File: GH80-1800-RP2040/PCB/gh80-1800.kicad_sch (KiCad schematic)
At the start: 280 parts, among them J1 USB_mini_micro_B, J2 ISP, J3 USB Header, J4 USB_mini_micro_B, J5 USB_mini_micro_B, K1 KEYSW, K10 KEYSW, K100 KEYSW, K101 KEYSW, K102 KEYSW, K103 KEYSW, K104 KEYSW, K105 KEYSW, K107 KEYSW, K108 KEYSW, K109 KEYSW, K11 KEYSW, K110 KEYSW, K12 KEYSW, K13 KEYSW, K14 KEYSW, K15 KEYSW, K16 KEYSW, K17 KEYSW, K18 KEYSW, K18-1 KEYSW, K19 KEYSW, K2 KEYSW, K20 KEYSW, K21 KEYSW, K22 KEYSW, K23 KEYSW, K24 KEYSW, K25 KEYSW, K26 KEYSW, K27 KEYSW, K28 KEYSW, K29 KEYSW, K3 KEYSW, K30 KEYSW, K31 KEYSW, K32 KEYSW, K33 KEYSW, K34 KEYSW, K35 KEYSW, K36 KEYSW, K37 KEYSW, K38 KEYSW, K39 KEYSW, K4 KEYSW, K40 KEYSW, K41 KEYSW, K42 KEYSW, K43 KEYSW, K44 KEYSW, K45 KEYSW, K46 KEYSW, K47 KEYSW, K48 KEYSW, K49 KEYSW, K5 KEYSW, K50 KEYSW, K51 KEYSW, K52 KEYSW, K53 KEYSW, K54 KEYSW, K55 KEYSW, K55-1 KEYSW, K56 KEYSW, K57 KEYSW, K58 KEYSW, K59 KEYSW, K6 KEYSW, K60 KEYSW, K61 KEYSW, K62 KEYSW, K63 KEYSW, K64 KEYSW, K65 KEYSW, K66 KEYSW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

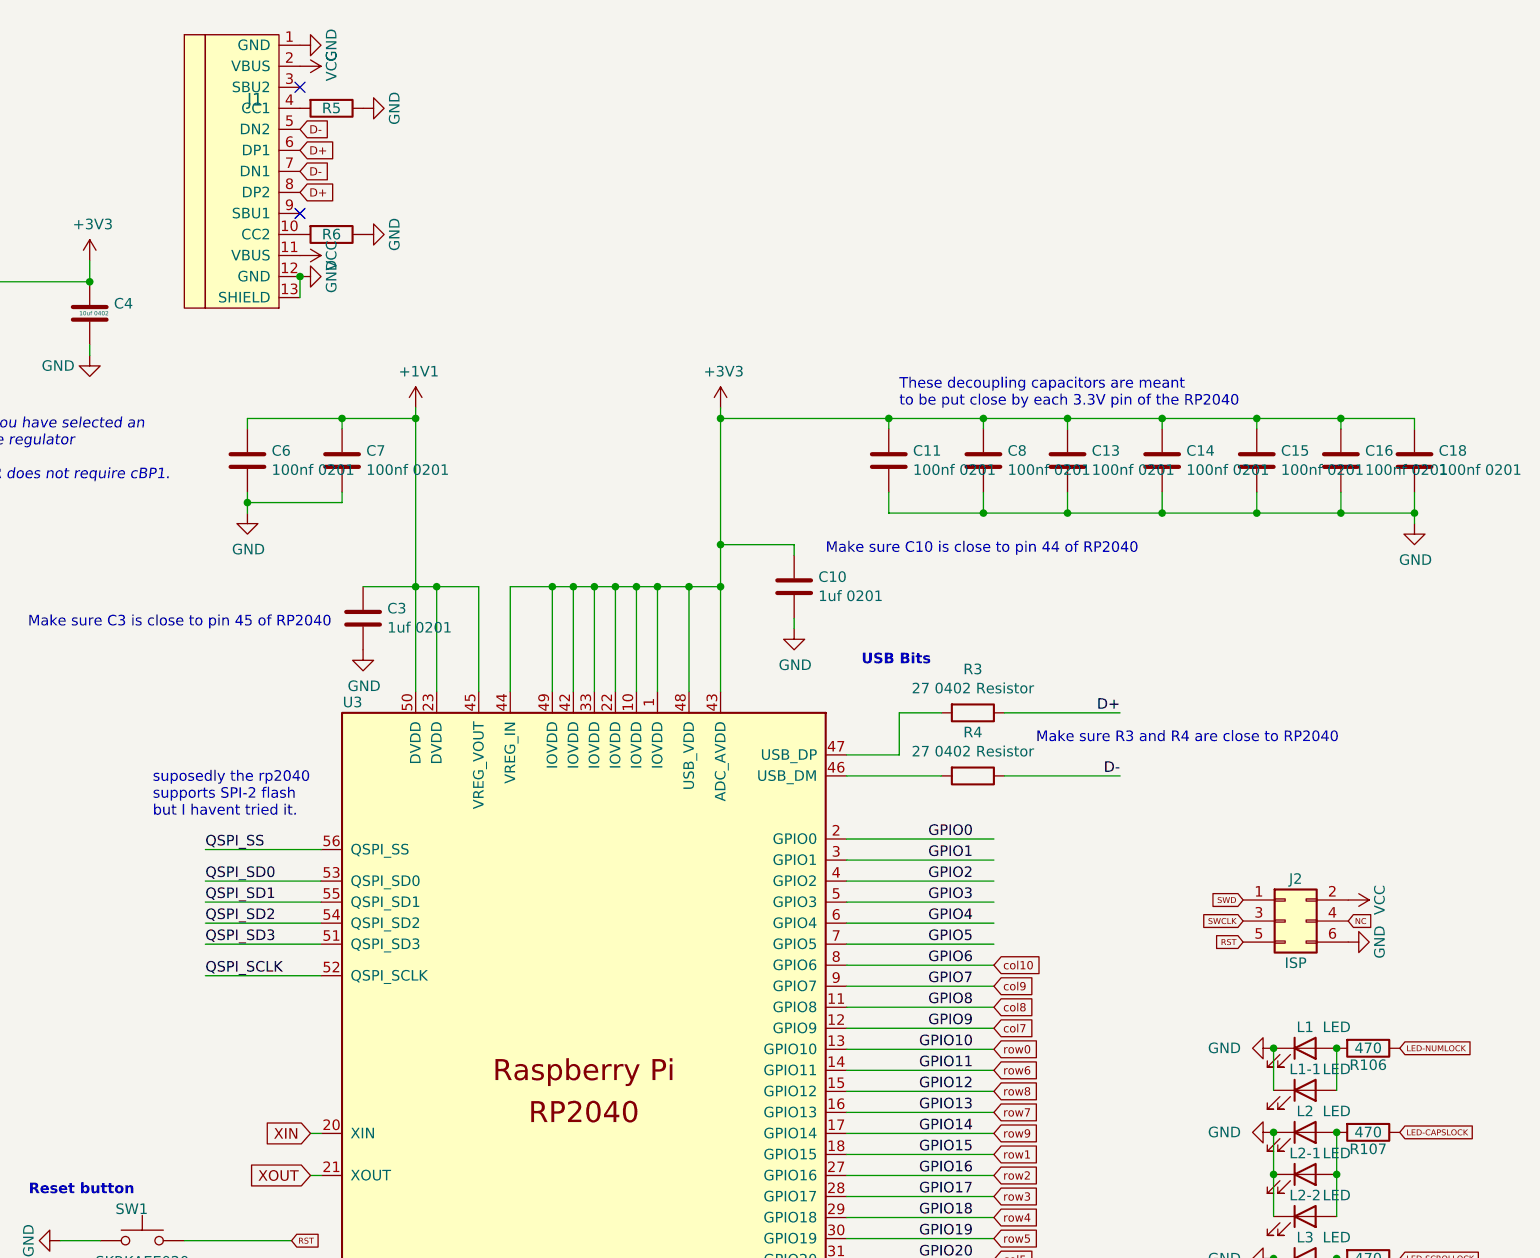
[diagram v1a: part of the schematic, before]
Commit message: remove unused bits from circuit
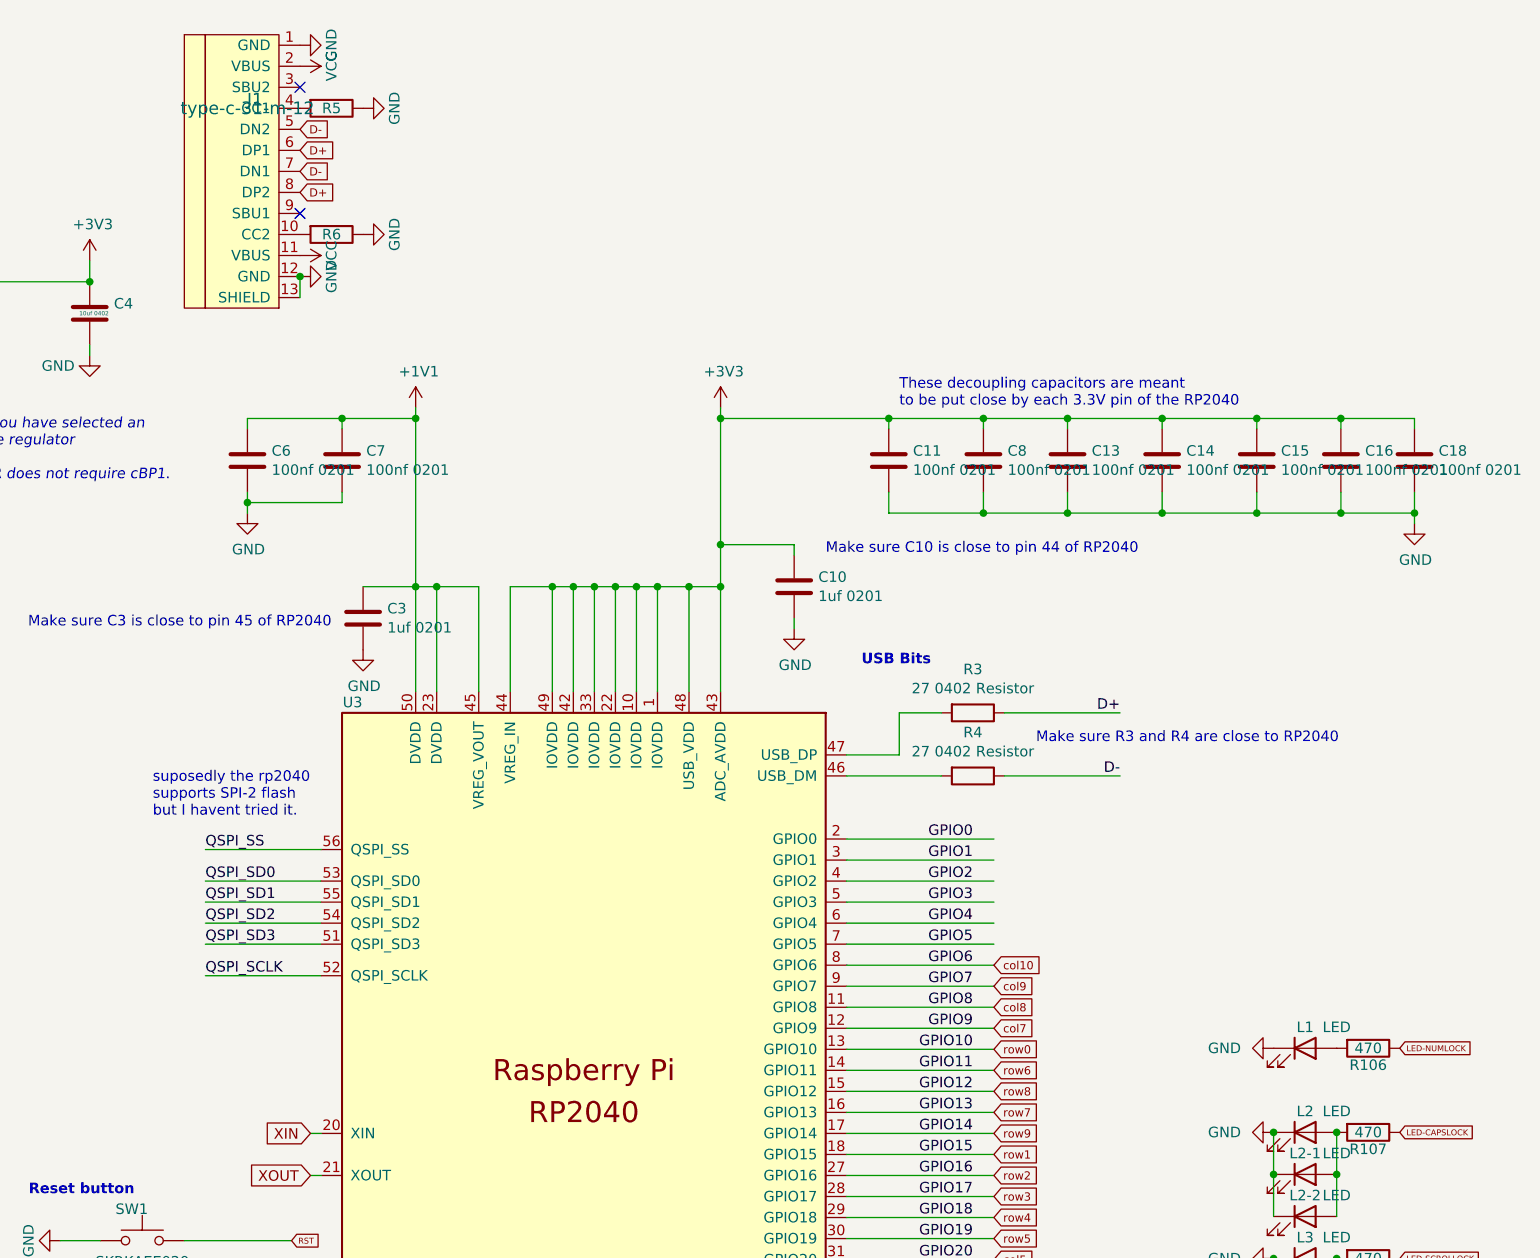
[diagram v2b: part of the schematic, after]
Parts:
- removed J2: ISP, Keeb_components:isp_standard, symbol Connector_Generic:Conn_02x03_Odd_Even
- removed L1-1: LED, Keeb_switches:CHERRY_MX_LED, symbol Device:LED
- J1: value USB_mini_micro_B -> type-c-31-m-12
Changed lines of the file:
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@@
   (junction (at 191.135 454.025) (diameter 0) (color 0 0 0 0)
   )
-  (junction (at 281.432 137.033) (diameter 0) (color 0 0 0 0)
-  )
   (junction (at 310.515 461.645) (diameter 0) (color 0 0 0 0)
   )
@@
   (junction (at 114.935 390.525) (diameter 0) (color 0 0 0 0)
   )
-  (junction (at 289.052 137.033) (diameter 0) (color 0 0 0 0)
-  )
   (junction (at 310.515 377.825) (diameter 0) (color 0 0 0 0)
   )
@@
     (stroke (width 0) (type default) (color 0 0 0 0))
   )
-  (wire (pts (xy 281.432 142.113) (xy 281.432 137.033))
-    (stroke (width 0) (type default) (color 0 0 0 0))
-  )
   (wire (pts (xy 353.695 471.805) (xy 353.695 476.885))
     (stroke (width 0) (type default) (color 0 0 0 0))
@@
     (stroke (width 0) (type default) (color 0 0 0 0))
   )
-  (wire (pts (xy 289.052 142.113) (xy 289.052 137.033))
-    (stroke (width 0) (type default) (color 0 0 0 0))
-  )
   (wire (pts (xy 254.635 390.525) (xy 226.695 390.525))
     (stroke (width 0) (type default) (color 0 0 0 0))
@@
     )
   )
-  (global_label "RST" (shape input) (at 277.749 124.206 180)
-    (effects (font (size 0.7112 0.7112)) (justify right))
-    (property "Intersheet References" "${INTERSHEET_REFS}" (id 0) (at 44.069 73.406 0)
-      (effects (font (size 1.27 1.27)) hide)
-    )
-  )
   (global_label "col2" (shape input) (at 163.195 332.105 0)
     (effects (font (size 1.4986 1.4986)) (justify left))
@@
     )
   )
-  (global_label "NC" (shape input) (at 290.449 121.666 0)
-    (effects (font (size 0.7112 0.7112)) (justify left))
-    (property "Intersheet References" "${INTERSHEET_REFS}" (id 0) (at 44.069 73.406 0)
-      (effects (font (size 0.7112 0.7112)) hide)
-    )
-  )
   (global_label "row4" (shape input) (at 247.65 157.48 0)
     (effects (font (size 0.9906 0.9906)) (justify left))
@@
     )
   )
-  (global_label "SWD" (shape input) (at 277.749 119.126 180)
-    (effects (font (size 0.7112 0.7112)) (justify right))
-    (property "Intersheet References" "${INTERSHEET_REFS}" (id 0) (at 44.069 73.406 0)
-      (effects (font (size 0.7112 0.7112)) hide)
-    )
-  )
   (global_label "VSYS" (shape input) (at 66.04 44.45 0) (fields_autoplaced)
     (effects (font (size 0.508 0.508)) (justify left))
@@
     )
   )
-  (global_label "SWCLK" (shape input) (at 277.749 121.666 180)
-    (effects (font (size 0.7112 0.7112)) (justify right))
-    (property "Intersheet References" "${INTERSHEET_REFS}" (id 0) (at 44.069 73.406 0)
-      (effects (font (size 0.7112 0.7112)) hide)
-    )
-  )
   (global_label "XIN" (shape input) (at 165.1 147.32 180) (fields_autoplaced)
     (effects (font (size 1.27 1.27)) (justify right))
@@
     (pin "1")
   )
-  (symbol (lib_id "Power:GND") (at 290.449 124.206 90) (unit 1)
-    (in_bom yes) (on_board yes)
-    (property "Reference" "#PWR010" (id 0) (at 296.799 124.206 0)
-      (effects (font (size 1.27 1.27)) hide)
-    )
-    (property "Value" "GND" (id 1) (at 294.259 124.206 0))
-    (property "Footprint" "" (id 2) (at 290.449 124.206 0)
-      (effects (font (size 1.27 1.27)) hide)
-    )
-    (property "Datasheet" "" (id 3) (at 290.449 124.206 0)
-      (effects (font (size 1.27 1.27)) hide)
-    )
-    (pin "1")
-  )
-  (symbol (lib_id "Power:VCC") (at 290.449 119.126 270) (unit 1)
-    (in_bom yes) (on_board yes)
-    (property "Reference" "#PWR011" (id 0) (at 286.639 119.126 0)
-      (effects (font (size 1.27 1.27)) hide)
-    )
-    (property "Value" "VCC" (id 1) (at 294.259 119.126 0))
-    (property "Footprint" "" (id 2) (at 290.449 119.126 0)
-      (effects (font (size 1.27 1.27)) hide)
-    )
-    (property "Datasheet" "" (id 3) (at 290.449 119.126 0)
-      (effects (font (size 1.27 1.27)) hide)
-    )
-    (pin "1")
-  )
-  (symbol (lib_id "Connector_Generic:Conn_02x03_Odd_Even") (at 282.829 121.666 0) (unit 1)
-    (in_bom yes) (on_board yes)
-    (property "Reference" "J2" (id 0) (at 284.099 116.586 0))
-    (property "Value" "ISP" (id 1) (at 284.099 126.746 0))
-    (property "Footprint" "Keeb_components:isp_standard" (id 2) (at 282.829 121.666 0)
-      (effects (font (size 1.27 1.27)) hide)
-    )
-    (property "Datasheet" "" (id 3) (at 282.829 121.666 0)
-      (effects (font (size 1.27 1.27)) hide)
-    )
-    (pin "1")
-    (pin "2")
-    (pin "3")
-    (pin "4")
-    (pin "5")
-    (pin "6")
-  )
   (symbol (lib_id "Device:LED") (at 285.242 137.033 0) (unit 1)
     (in_bom yes) (on_board yes)
@@
       (effects (font (size 1.524 1.524)))
     )
-    (property "Value" "USB_mini_micro_B" (id 1) (at 157.48 23.495 0)
-      (effects (font (size 1.524 1.524)) hide)
+    (property "Value" "type-c-31-m-12" (id 1) (at 157.48 23.495 0)
+      (effects (font (size 1.524 1.524)))
     )
     (property "Footprint" "Type-C:HRO-TYPE-C-31-M-12" (id 2) (at 161.29 29.845 0)
@@
     (pin "2")
   )
-  (symbol (lib_id "Device:LED") (at 285.242 142.113 0) (unit 1)
-    (in_bom yes) (on_board yes)
-    (property "Reference" "L1-1" (id 0) (at 285.242 139.573 0))
-    (property "Value" "LED" (id 1) (at 289.052 139.573 0))
-    (property "Footprint" "Keeb_switches:CHERRY_MX_LED" (id 2) (at 285.242 142.113 0)
-      (effects (font (size 1.27 1.27)) hide)
-    )
-    (property "Datasheet" "" (id 3) (at 285.242 142.113 0)
-      (effects (font (size 1.27 1.27)) hide)
-    )
-    (pin "1")
-    (pin "2")
-  )
   (symbol (lib_id "keyboard_parts:KEYSW") (at 374.015 426.085 0) (unit 1)
     (in_bom yes) (on_board yes)
@@
       (reference "#PWR09") (unit 1) (value "+3V3") (footprint "")
     )
-    (path "/00000000-0000-0000-0000-000059ee9bff"
-      (reference "#PWR010") (unit 1) (value "GND") (footprint "")
-    )
-    (path "/00000000-0000-0000-0000-000059ee9e32"
-      (reference "#PWR011") (unit 1) (value "VCC") (footprint "")
-    )
     (path "/00000000-0000-0000-0000-00005edc8ac7"
       (reference "#PWR015") (unit 1) (value "GND") (footprint "")
@@
     )
     (path "/00000000-0000-0000-0000-00005bd01273"
-      (reference "J1") (unit 1) (value "USB_mini_micro_B") (footprint "Type-C:HRO-TYPE-C-31-M-12")
-    )
-    (path "/00000000-0000-0000-0000-00005a55f774"
-      (reference "J2") (unit 1) (value "ISP") (footprint "Keeb_components:isp_standard")
+      (reference "J1") (unit 1) (value "type-c-31-m-12") (footprint "Type-C:HRO-TYPE-C-31-M-12")
     )
     (path "/00000000-0000-0000-0000-00005b4e3031"
@@
       (reference "L1") (unit 1) (value "LED") (footprint "Keeb_components:LED_D3.0mm")
     )
-    (path "/00000000-0000-0000-0000-00005c91ee53"
-      (reference "L1-1") (unit 1) (value "LED") (footprint "Keeb_switches:CHERRY_MX_LED")
-    )
     (path "/00000000-0000-0000-0000-00005b0d3b7c"
